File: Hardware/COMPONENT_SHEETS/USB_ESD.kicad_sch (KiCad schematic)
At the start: 10 parts, among them J4 10118192-0001LF, U3 LP38692MPX-ADJ, U4 USBLC6-2SC6

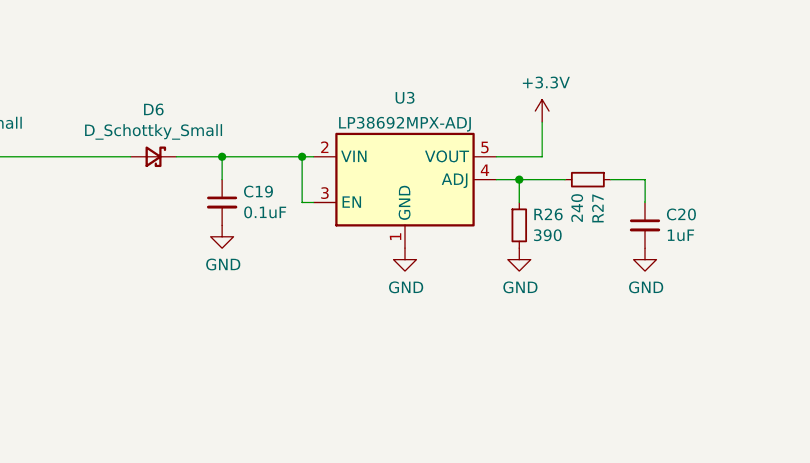
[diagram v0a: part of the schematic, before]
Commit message: corrected voltage regulator footprint
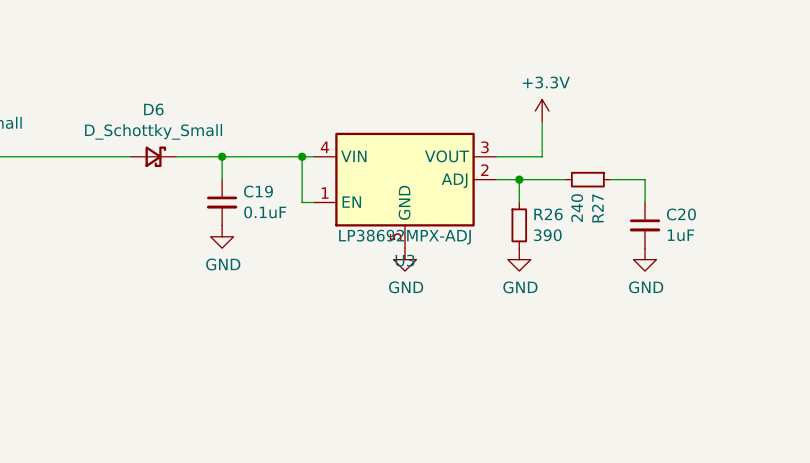
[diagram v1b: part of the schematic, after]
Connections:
- net +3V3: now also U3.3 (VOUT); no longer U3.5 (VOUT)
- net GND: now also U3.5 (GND); no longer U3.1 (GND)
- net at R26.1, R27.2: now also U3.2 (ADJ); no longer U3.4 (ADJ)
- net at C19.1, D6.1 (K): now also U3.1 (EN), U3.4 (VIN); no longer U3.2 (VIN), U3.3 (EN)
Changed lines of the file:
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@@
   (symbol (lib_id "Regulator_Linear:ADP7182AUJZ") (at 147.32 85.09 0) (mirror x) (unit 1)
     (in_bom yes) (on_board yes) (fields_autoplaced)
-    (property "Reference" "U3" (id 0) (at 147.32 76.0435 0))
-    (property "Value" "LP38692MPX-ADJ" (id 1) (at 147.32 78.8186 0))
-    (property "Footprint" "Package_TO_SOT_SMD:SOT-223-5" (id 2) (at 147.32 74.93 0)
+    (property "Reference" "U3" (id 0) (at 147.32 94.1365 0))
+    (property "Value" "LP38692MPX-ADJ" (id 1) (at 147.32 91.3614 0))
+    (property "Footprint" "Package_TO_SOT_SMD:SOT-223-5" (id 2) (at 147.32 95.25 0)
       (effects (font (size 1.27 1.27) italic) hide)
     )
-    (property "Datasheet" "https://media.digikey.com/pdf/Data%20Sheets/Texas%20Instruments%20PDFs/LP38690,92-ADJ.pdf" (id 3) (at 147.32 72.39 0)
+    (property "Datasheet" "https://media.digikey.com/pdf/Data%20Sheets/Texas%20Instruments%20PDFs/LP38690,92-ADJ.pdf" (id 3) (at 147.32 97.79 0)
       (effects (font (size 1.27 1.27)) hide)
     )
